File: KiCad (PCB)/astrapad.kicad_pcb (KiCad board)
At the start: 2 copper layers, 99.9 x 54.8 mm, 34 parts, among them J1 Astras Glasses, SW1 SW_Push, SW13 RotaryEncoder_Switch, SW2 SW_Push, SW3 SW_Push, SW5 SW_Push, SW6 SW_Push, SW7 SW_Push, SW8 SW_Push, U1 XIAO-RP2040-DIP

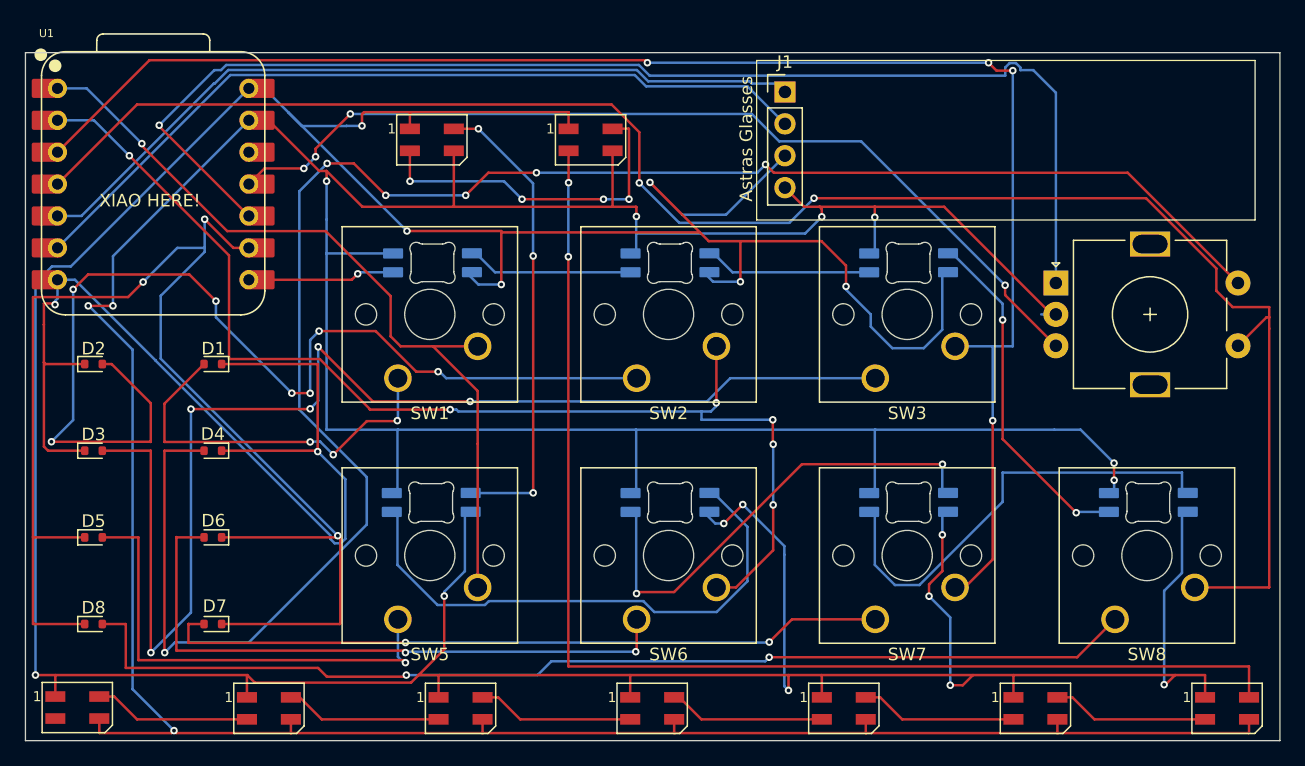
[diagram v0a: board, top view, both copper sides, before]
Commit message: Added some silkscreens
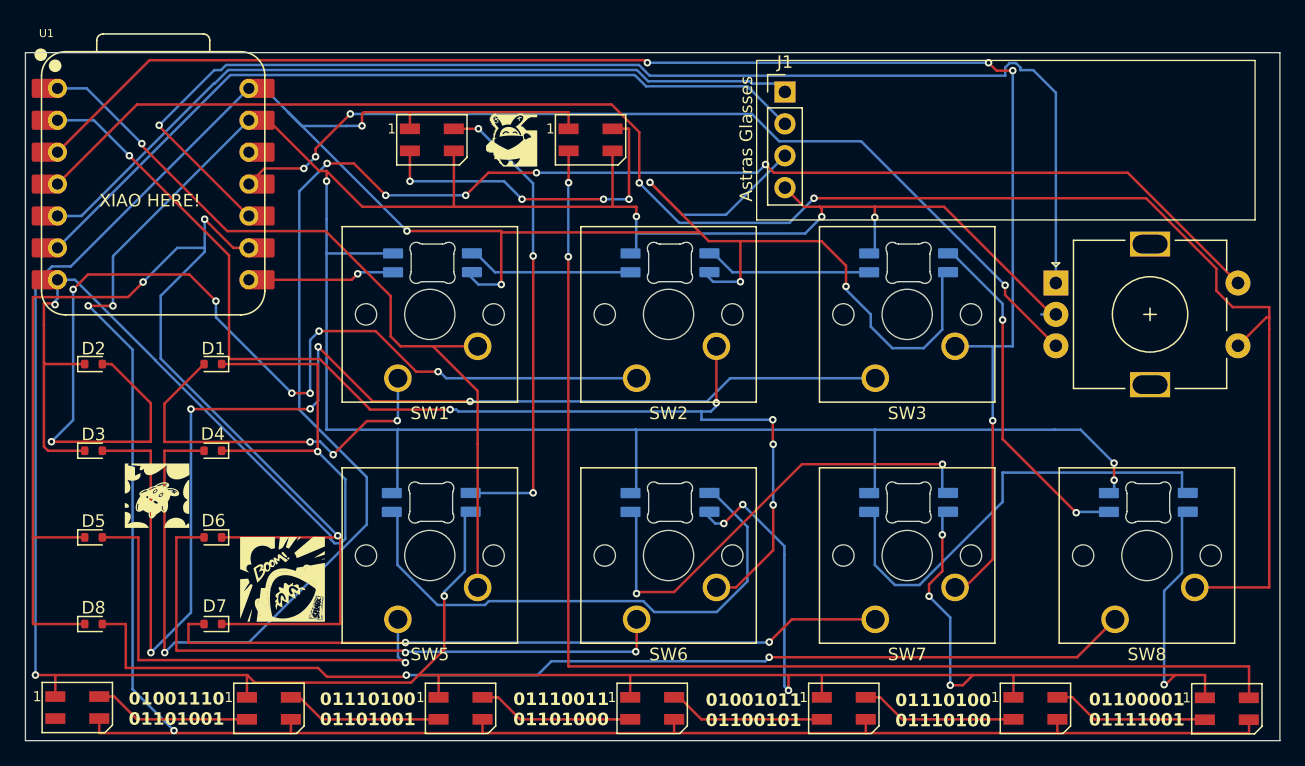
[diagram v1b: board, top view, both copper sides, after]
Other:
- board text added: "01001011 01100101"
- board text added: "01001110 01101001"
- board text added: "01100001 01111001"
- board text added: "01110011 01101000"
- board text added: "01110100 01101001"
- board text added: "01110100 01110100"
